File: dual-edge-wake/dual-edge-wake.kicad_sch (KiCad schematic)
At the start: 14 parts, among them Q1 BC327, Q2 2N3904, Q3 2N3904, U1 XOR

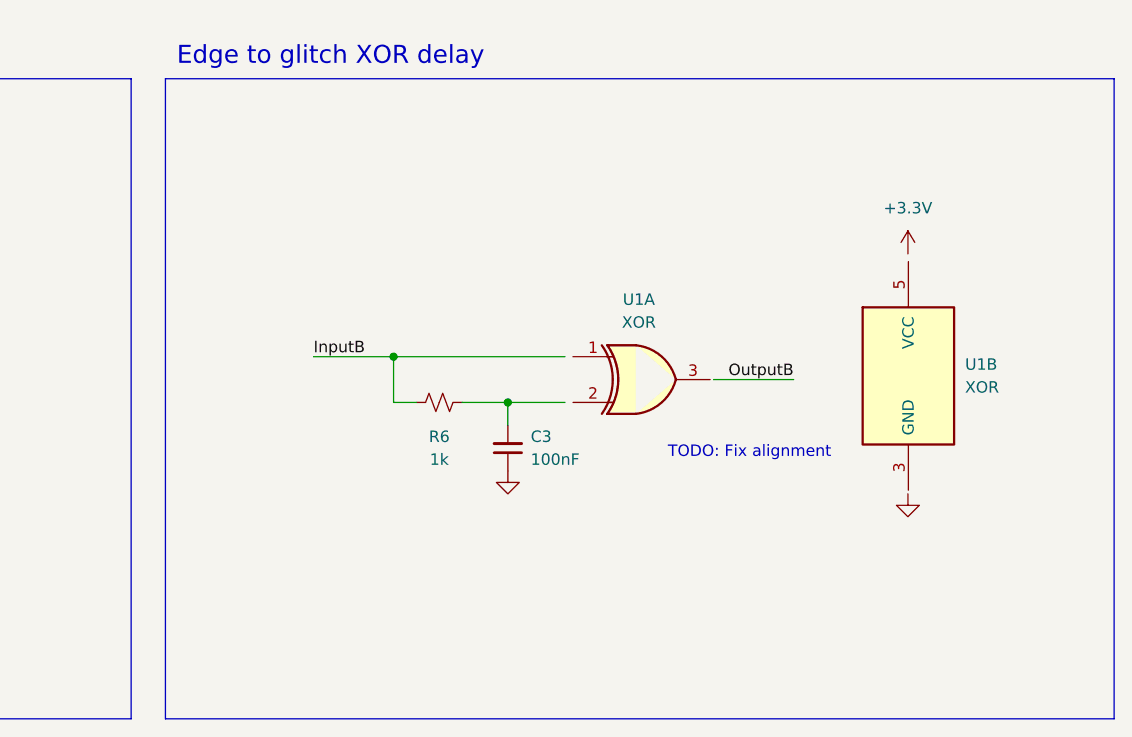
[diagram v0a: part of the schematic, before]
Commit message: Add custom RC jumper
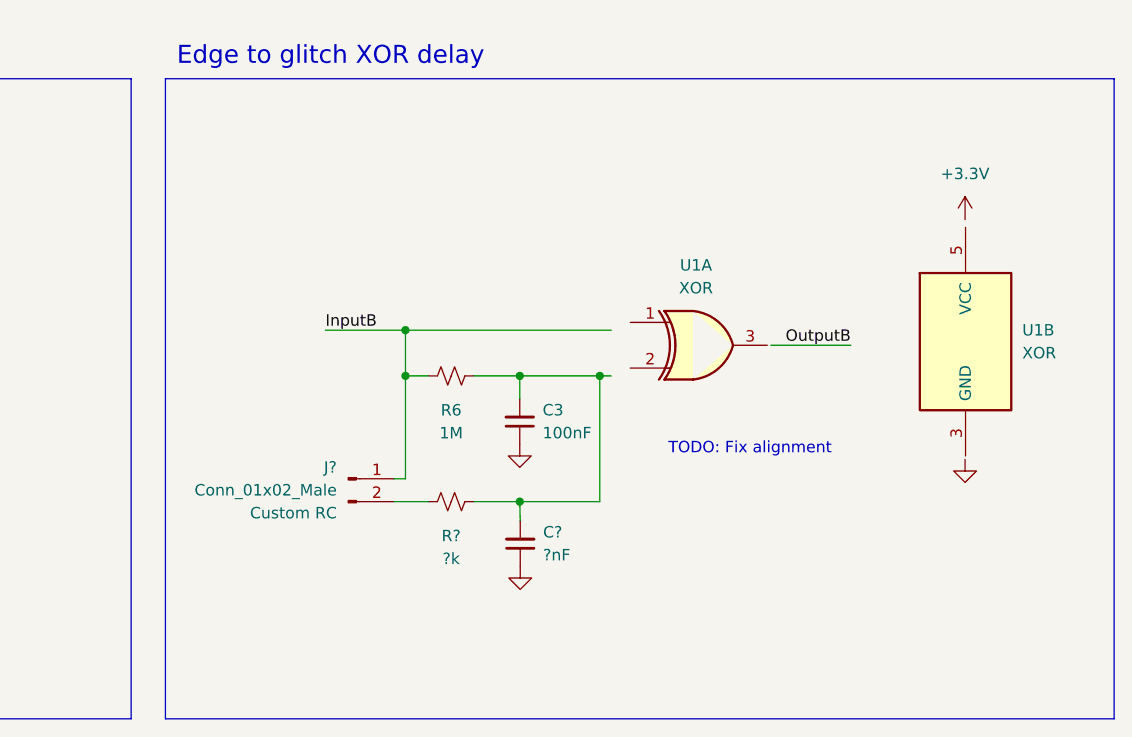
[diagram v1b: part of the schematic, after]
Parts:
- added C?: ?nF, Capacitor_THT:C_Disc_D5.0mm_W2.5mm_P2.50mm, symbol Device:C_Small
- added J?: Conn_01x02_Male, symbol Connector:Conn_01x02_Male
- added R?: ?k, Resistor_THT:R_Axial_DIN0207_L6.3mm_D2.5mm_P7.62mm_Horizontal, symbol Device:R_Small_US
- J?: footprint Connector_JST:JST_XH_B2B-XH-A_1x02_P2.50mm_Vertical -> (none)
- R6: value 1k -> 1M
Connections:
- net GND: now also C?.1
- net InputB: now also J?.1 (Pin_1)
- net at C3.2, R6.1: now also C?.2, R?.1
- new net: J?.2 (Pin_2), R?.2
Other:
- moved on the sheet: C3, R6, U1A, U1B

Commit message: Assign value to XOR
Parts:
- U1: value XOR -> M74VHC1GT86DTT1G; footprint (none) -> Package_TO_SOT_SMD:SOT-23-5_HandSoldering
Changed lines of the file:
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@@
     (in_bom yes) (on_board yes) (fields_autoplaced)
     (property "Reference" "U1" (id 0) (at 220.2432 93.1164 0))
-    (property "Value" "XOR" (id 1) (at 220.2432 95.6564 0))
-    (property "Footprint" "" (id 2) (at 215.8492 96.9264 0)
-      (effects (font (size 1.27 1.27)) hide)
-    )
-    (property "Datasheet" "" (id 3) (at 215.8492 96.9264 0)
+    (property "Value" "M74VHC1GT86DTT1G" (id 1) (at 220.2432 95.6564 0))
+    (property "Footprint" "Package_TO_SOT_SMD:SOT-23-5_HandSoldering" (id 2) (at 215.8492 96.9264 0)
+      (effects (font (size 1.27 1.27)) hide)
+    )
+    (property "Datasheet" "https://www.farnell.com/datasheets/1577687.pdf" (id 3) (at 215.8492 96.9264 0)
       (effects (font (size 1.27 1.27)) hide)
     )
@@
       (effects (font (size 1.27 1.27)) (justify left))
     )
-    (property "Value" "XOR" (id 1) (at 256.4892 102.8699 0)
-      (effects (font (size 1.27 1.27)) (justify left))
-    )
-    (property "Footprint" "" (id 2) (at 247.5992 96.9264 0)
-      (effects (font (size 1.27 1.27)) hide)
-    )
-    (property "Datasheet" "" (id 3) (at 247.5992 96.9264 0)
+    (property "Value" "M74VHC1GT86DTT1G" (id 1) (at 256.4892 102.8699 0)
+      (effects (font (size 1.27 1.27)) (justify left))
+    )
+    (property "Footprint" "Package_TO_SOT_SMD:SOT-23-5_HandSoldering" (id 2) (at 247.5992 96.9264 0)
+      (effects (font (size 1.27 1.27)) hide)
+    )
+    (property "Datasheet" "https://www.farnell.com/datasheets/1577687.pdf" (id 3) (at 247.5992 96.9264 0)
       (effects (font (size 1.27 1.27)) hide)
     )
@@
     )
     (path "/80885ac7-b5dc-4c53-80ea-fe4770c448b7"
-      (reference "U1") (unit 1) (value "XOR") (footprint "")
+      (reference "U1") (unit 1) (value "M74VHC1GT86DTT1G") (footprint "Package_TO_SOT_SMD:SOT-23-5_HandSoldering")
     )
     (path "/832fc88c-fb68-48c9-a677-76e4a12d8cc4"
-      (reference "U1") (unit 2) (value "XOR") (footprint "")
-    )
-  )
+      (reference "U1") (unit 2) (value "M74VHC1GT86DTT1G") (footprint "Package_TO_SOT_SMD:SOT-23-5_HandSoldering")
+    )
+  )

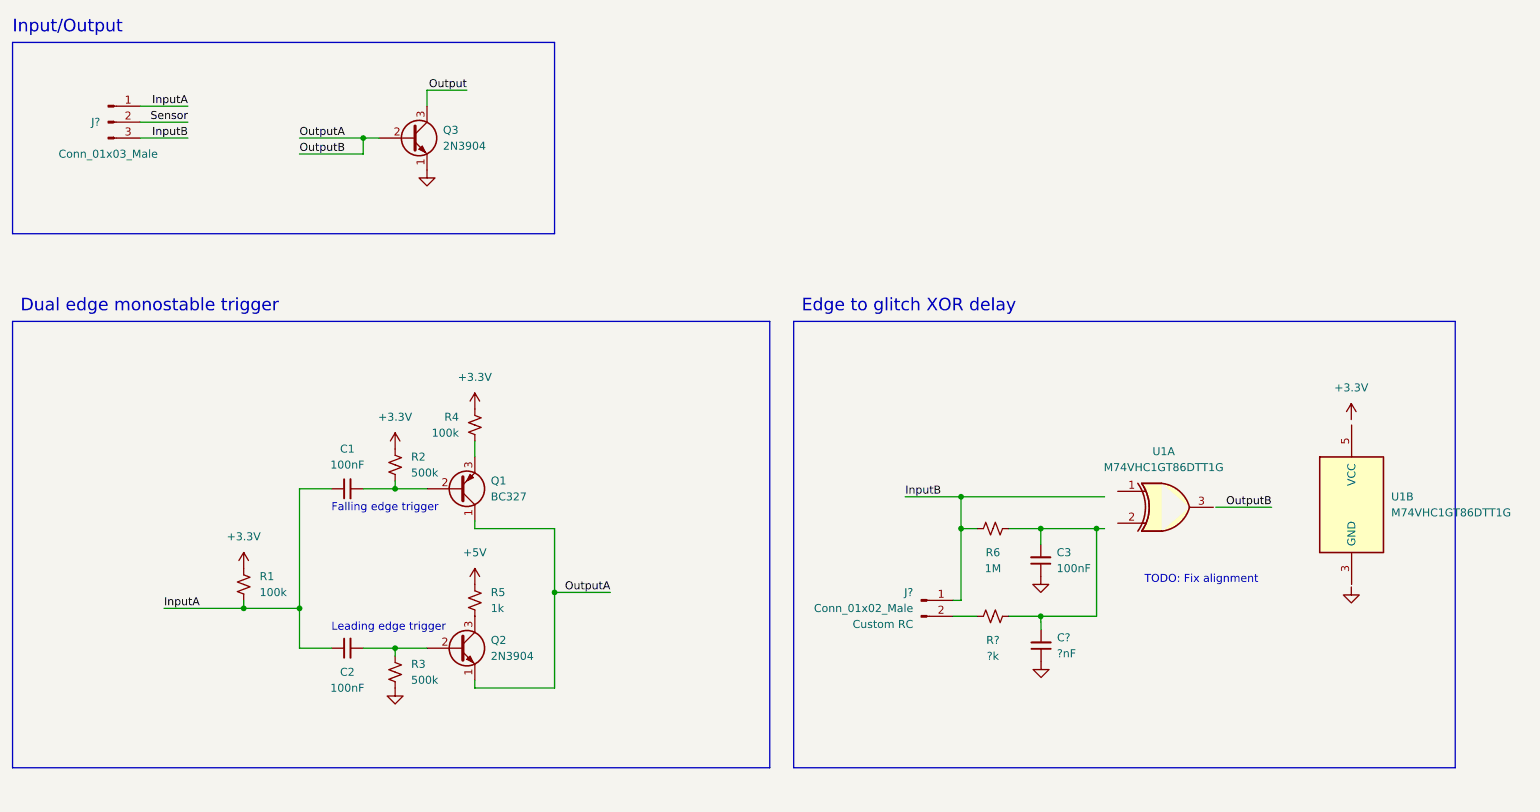
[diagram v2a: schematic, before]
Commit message: Assigned footprints and started PCB
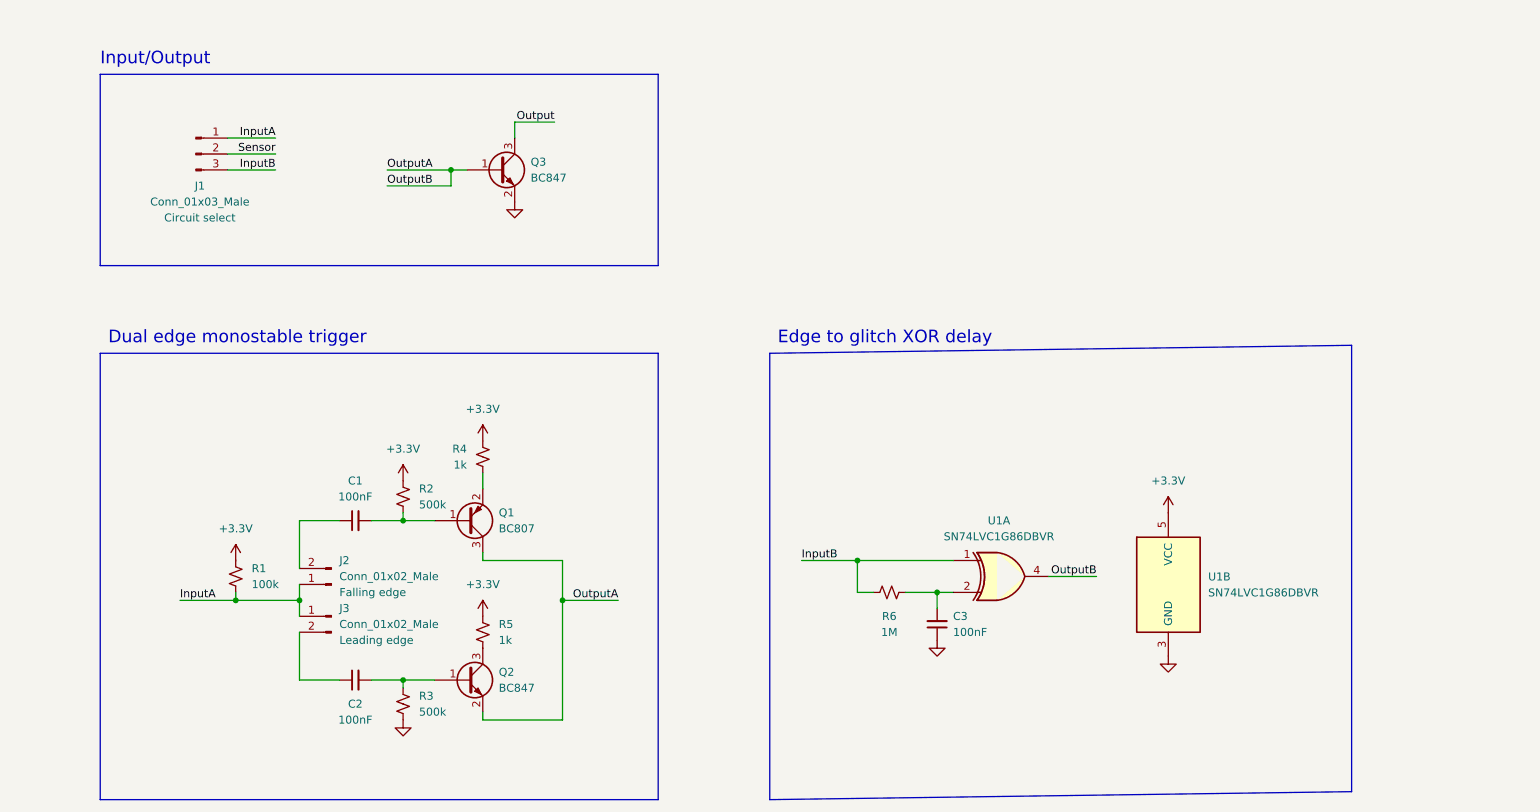
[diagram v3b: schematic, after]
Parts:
- removed C?: ?nF, Capacitor_THT:C_Disc_D5.0mm_W2.5mm_P2.50mm, symbol Device:C_Small
- removed J?: Conn_01x02_Male, symbol Connector:Conn_01x02_Male
- removed Q1: BC327, Package_TO_SOT_THT:TO-92_Inline, symbol Transistor_BJT:BC327
- removed Q2, Q3: 2N3904, Package_TO_SOT_THT:TO-92_Inline, symbol Transistor_BJT:2N3904
- removed R?: ?k, Resistor_THT:R_Axial_DIN0207_L6.3mm_D2.5mm_P7.62mm_Horizontal, symbol Device:R_Small_US
- removed unit 2 of U1
- added J2, J3: Conn_01x02_Male, Jumper:SolderJumper-2_P1.3mm_Open_RoundedPad1.0x1.5mm, symbol Connector:Conn_01x02_Male
- added Q1: BC807, Package_TO_SOT_SMD:SOT-23_Handsoldering, symbol Transistor_BJT:BC807
- added Q2, Q3: BC847, Package_TO_SOT_SMD:SOT-23_Handsoldering, symbol Transistor_BJT:BC847
- added unit 2 of U1
- C1, C2, C3: footprint Capacitor_THT:C_Disc_D5.0mm_W2.5mm_P2.50mm -> Capacitor_SMD:C_0805_2012Metric_Pad1.18x1.45mm_HandSolder; LCSC (none) -> C1711
- J1: renamed from J?; footprint (none) -> Jumper:SolderJumper-3_P1.3mm_Open_RoundedPad1.0x1.5mm; A (none) -> Dual edge monostable trigger; B (none) -> Edge to glitch XOR delay; Label (none) -> Circuit select; now left out of the parts list
- R1: footprint Resistor_THT:R_Axial_DIN0207_L6.3mm_D2.5mm_P7.62mm_Horizontal -> Resistor_SMD:R_0603_1608Metric_Pad0.98x0.95mm_HandSolder; LCSC (none) -> C180850
- R2, R3: footprint Resistor_THT:R_Axial_DIN0207_L6.3mm_D2.5mm_P7.62mm_Horizontal -> Resistor_SMD:R_0603_1608Metric_Pad0.98x0.95mm_HandSolder; LCSC (none) -> C2077866
- R4: value 100k -> 1k; footprint Resistor_THT:R_Axial_DIN0207_L6.3mm_D2.5mm_P7.62mm_Horizontal -> Resistor_SMD:R_0603_1608Metric_Pad0.98x0.95mm_HandSolder; LCSC (none) -> C79496
- R5: footprint Resistor_THT:R_Axial_DIN0207_L6.3mm_D2.5mm_P7.62mm_Horizontal -> Resistor_SMD:R_0603_1608Metric_Pad0.98x0.95mm_HandSolder; LCSC (none) -> C79496
- R6: footprint Resistor_THT:R_Axial_DIN0207_L6.3mm_D2.5mm_P7.62mm_Horizontal -> Resistor_SMD:R_0603_1608Metric_Pad0.98x0.95mm_HandSolder; LCSC (none) -> C413339
- U1: value M74VHC1GT86DTT1G -> SN74LVC1G86DBVR; symbol Nick:XOR -> Nick:SN74LVC1G86DBVR; LCSC (none) -> C402161
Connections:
- net +5V is gone; now on net +3.3V: R5.1
- net +3.3V: now also U1.5 (VCC)
- net GND: now also Q3.2 (E), U1.3 (GND)
- net InputA: now also J2.1 (Pin_1), J3.1 (Pin_1); no longer C1.1, C2.1
- net InputB: now also U1.1
- net Output: now also Q3.3 (C)
- net OutputA: now also U1.4, Q1.3 (C), Q2.2 (E), Q3.1 (B)
- net at C3.2, R6.1: now also U1.2
- net at C2.2, R3.2: now also Q2.1 (B)
- net at C1.2, R2.2: now also Q1.1 (B)
- net at R4.2: now also Q1.2 (E)
- net at R5.2: now also Q2.3 (C)
- new net: C2.1, J3.2 (Pin_2)
- new net: C1.1, J2.2 (Pin_2)
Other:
- note removed: "Falling edge trigger"
- note removed: "Leading edge trigger"
- note removed: "TODO: Fix alignment"
- company: (none) -> Nick Bolton
- title: (none) -> ESP8266 dual edge wake
- moved on the sheet: C1, C2, C3, J1, R1, R2, R3, R4, R5, R6, U1A

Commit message: Finished first PCB
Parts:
- added J1: Conn_01x04_Male, Connector_PinHeader_2.54mm:PinHeader_1x04_P2.54mm_Vertical, symbol Connector:Conn_01x04_Male
- J2: renamed from J1; value Conn_01x03_Male -> Circuit; A Dual edge monostable trigger -> (none); B Edge to glitch XOR delay -> (none); Label Circuit select -> (none)
- J3: renamed from J2; value Conn_01x02_Male -> Falling; Label Falling edge -> (none)
- J4: renamed from J3; value Conn_01x02_Male -> Leading; Label Leading edge -> (none)
- R1, R2, R3, R4, R5, R6: footprint Resistor_SMD:R_0603_1608Metric_Pad0.98x0.95mm_HandSolder -> Resistor_SMD:R_0805_2012Metric_Pad1.20x1.40mm_HandSolder
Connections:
- net +3.3V: now also J1.1 (Pin_1)
- net GND: now also J1.2 (Pin_2)
- net Output: now also J1.4 (Pin_4)
- net InputA renamed A
- net InputB renamed B
- net OutputA renamed C
- net Sensor renamed Input
- net Input: now also J1.3 (Pin_3)
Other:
- moved on the sheet: J2, Q3
